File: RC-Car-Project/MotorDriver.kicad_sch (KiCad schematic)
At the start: 0 parts

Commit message: Add libraries and components in schs
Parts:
- added Q1, Q2: BTN8982TA, Package_TO_SOT_SMD:TO-263-7_TabPin8, symbol Power_Management:BTN8982TA
- added U9: SN74HC244PWR, PW20, symbol SN74HC244PWR:SN74HC244PWR
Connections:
- new net: Q2.4, Q2.8
- new net: Q1.4, Q1.8

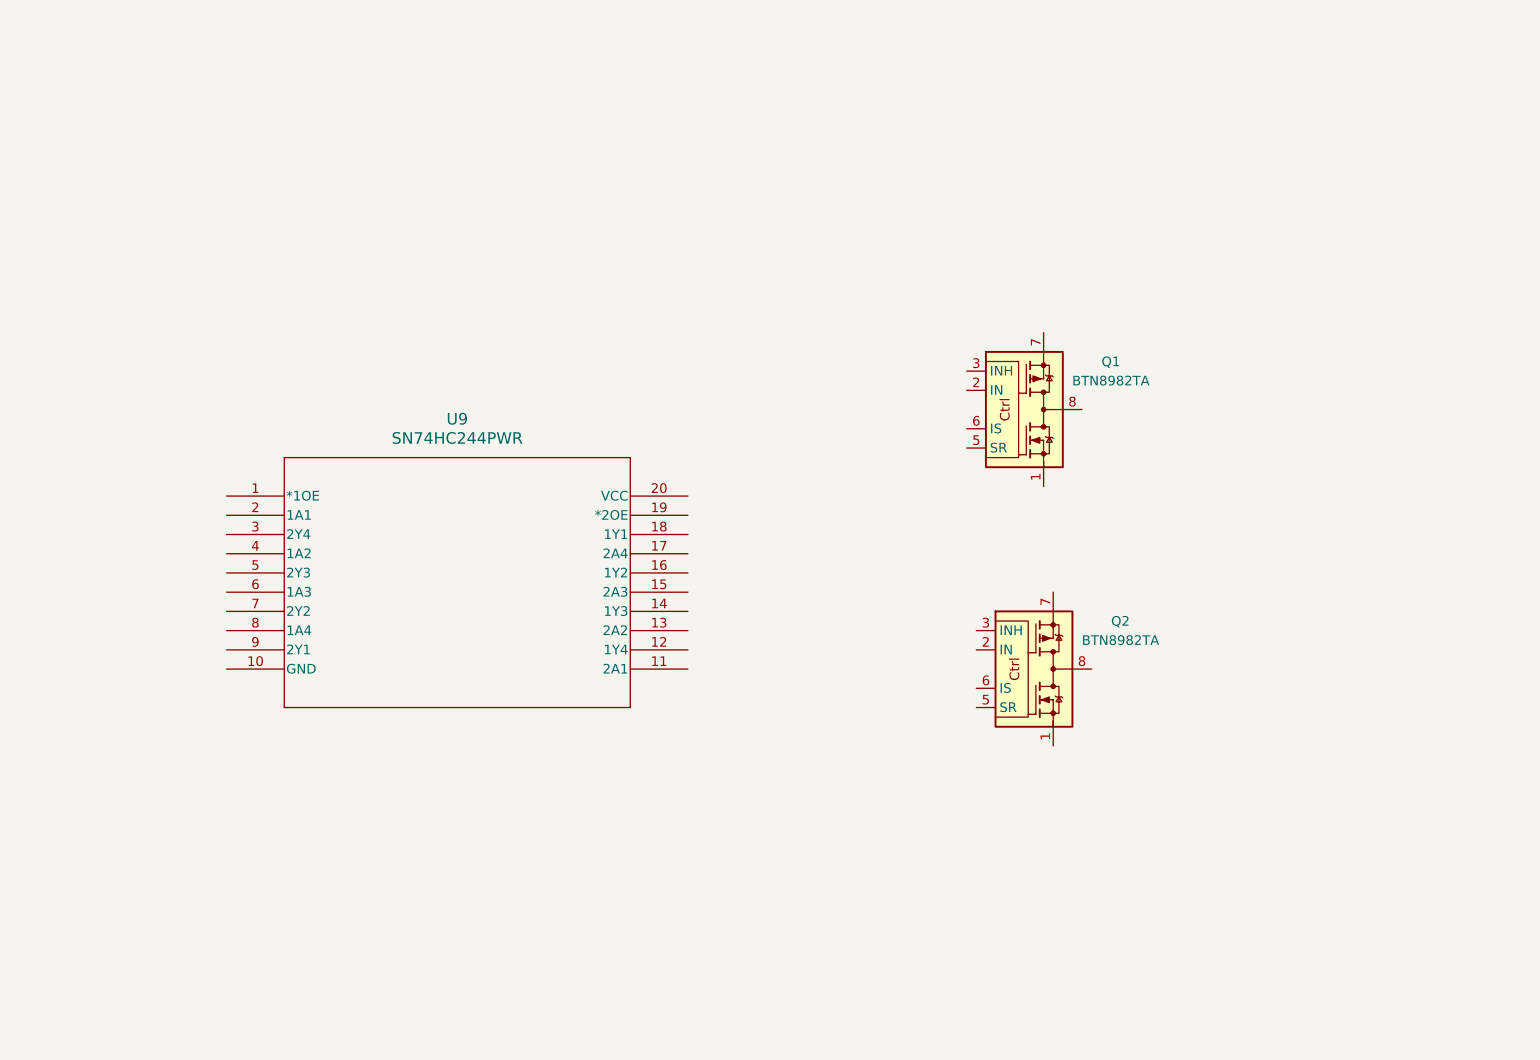
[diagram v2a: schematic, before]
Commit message: Added Basic Schematic + STM32 Project config. TODO: Component value selection + double check all connections.
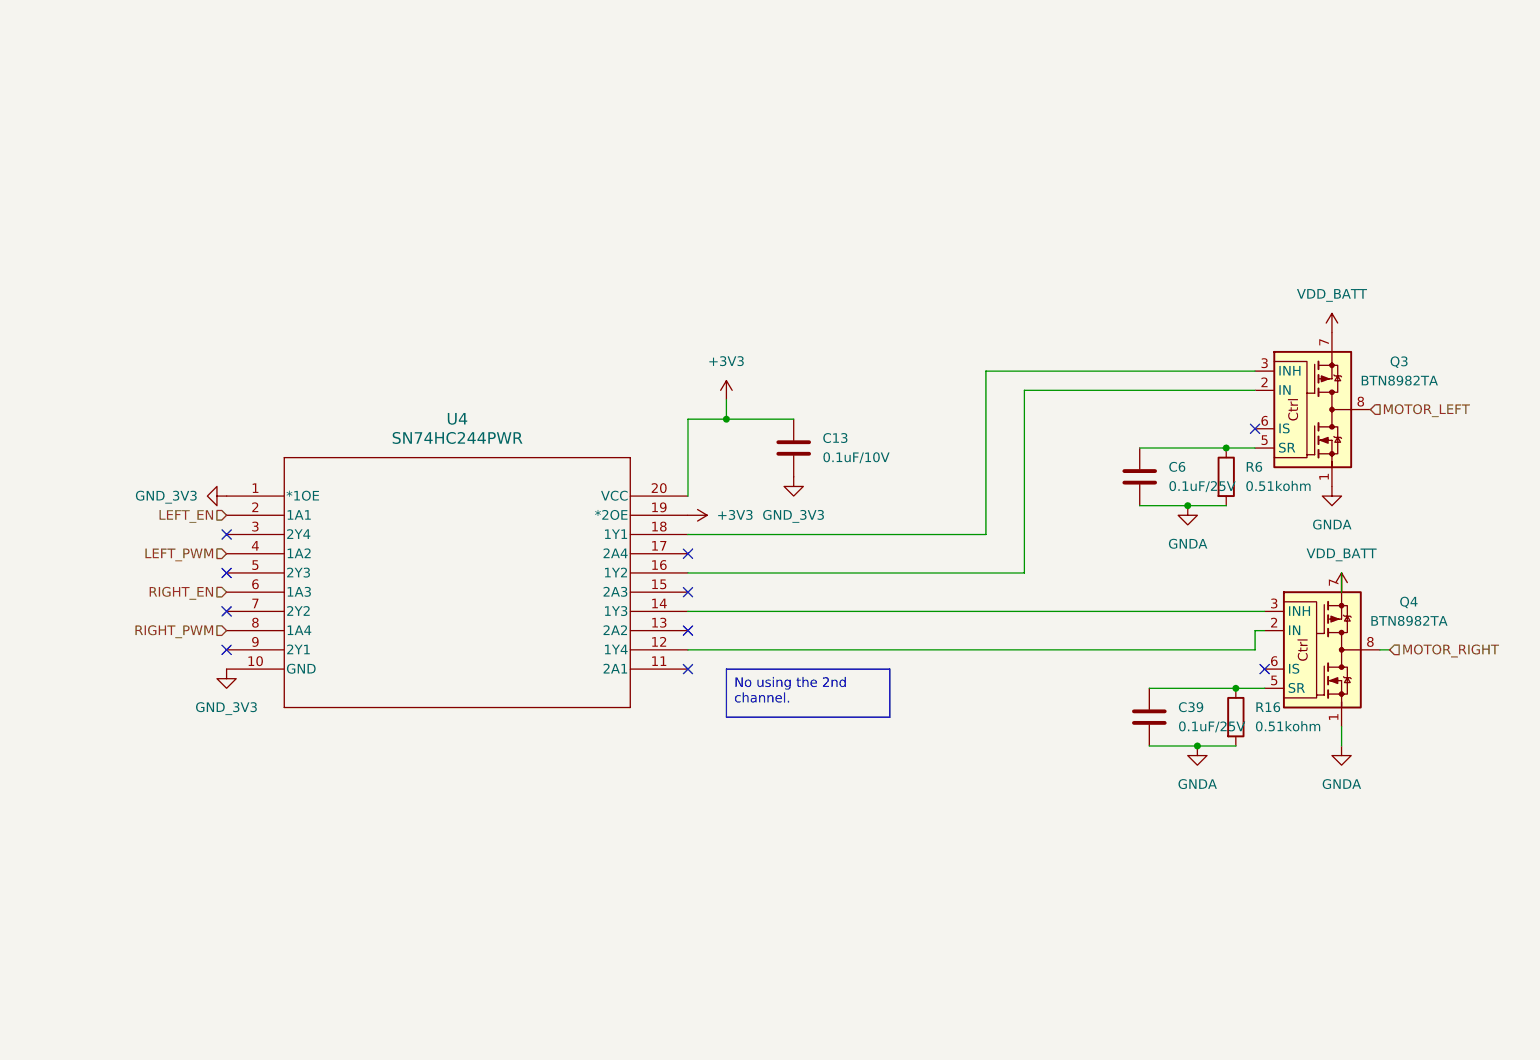
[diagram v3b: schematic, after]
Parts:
- added C13: 0.1uF/10V, symbol Device:C
- added C39, C6: 0.1uF/25V, symbol Device:C
- added R16, R6: 0.51kohm, symbol Device:R
- renumbered Q1 to Q3, Q2 to Q4, U9 to U4
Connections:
- net GNDA: now reaches Q4.1
- net GNDA: now also Q3.1, C39.2, C6.2, R16.2, R6.2
- net at Q4.2 (IN): now also U4.12 (1Y4)
- net at Q4.3 (INH): now also U4.14 (1Y3)
- net MOTOR_RIGHT: now reaches Q4.4, Q4.8
- net at Q4.5 (SR): now also C39.1, R16.1
- net VDD_BATT: now reaches Q4.7
- net VDD_BATT: now also Q3.7
- net at Q3.2 (IN): now also U4.16 (1Y2)
- net at Q3.3 (INH): now also U4.18 (1Y1)
- net MOTOR_LEFT: now reaches Q3.4, Q3.8
- net at Q3.5 (SR): now also C6.1, R6.1
- net GND_3V3: now reaches U4.1 (*1OE)
- net GND_3V3: now also U4.10 (GND), C13.2
- net +3V3: now reaches U4.19 (*2OE)
- net +3V3: now also U4.20 (VCC), C13.1
- net LEFT_EN: now reaches U4.2 (1A1)
- net LEFT_PWM: now reaches U4.4 (1A2)
- net RIGHT_EN: now reaches U4.6 (1A3)
- net RIGHT_PWM: now reaches U4.8 (1A4)
- no-connect marks 0 -> 10
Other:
- moved on the sheet: Q3, Q4

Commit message: Cleaned up Motor Circuit
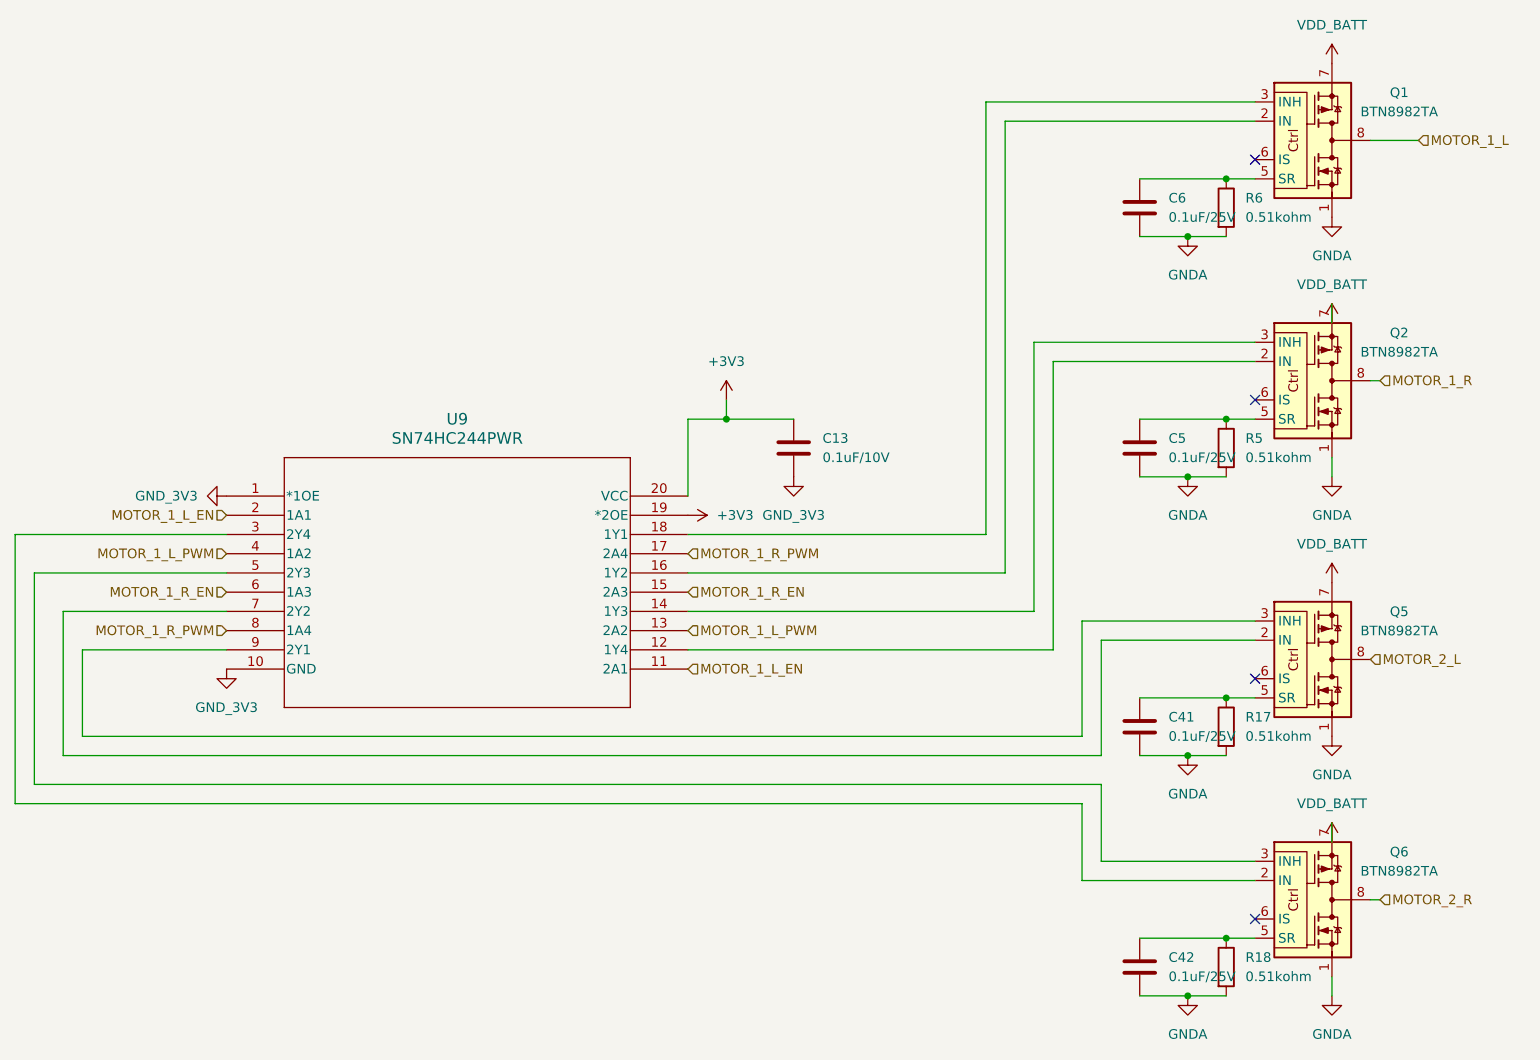
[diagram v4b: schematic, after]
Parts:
- added C41, C42: 0.1uF/25V, symbol Device:C
- added Q5, Q6: BTN8982TA, Package_TO_SOT_SMD:TO-263-7_TabPin8, symbol Power_Management:BTN8982TA
- added R17, R18: 0.51kohm, symbol Device:R
- renumbered C39 to C5, Q3 to Q1, Q4 to Q2, R16 to R5, U4 to U9
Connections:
- net LEFT_EN is gone; now on net MOTOR_1_L_EN: U9.2 (1A1)
- net LEFT_PWM is gone; now on net MOTOR_1_L_PWM: U9.4 (1A2)
- net RIGHT_EN is gone; now on net MOTOR_1_R_EN: U9.6 (1A3)
- net RIGHT_PWM is gone; now on net MOTOR_1_R_PWM: U9.8 (1A4)
- net GNDA: now also C41.2, C42.2, Q5.1, Q6.1, R17.2, R18.2
- net VDD_BATT: now also Q5.7, Q6.7
- net MOTOR_1_L_EN: now reaches U9.11 (2A1)
- net MOTOR_1_L_PWM: now reaches U9.13 (2A2)
- net MOTOR_1_R_EN: now reaches U9.15 (2A3)
- net MOTOR_1_R_PWM: now reaches U9.17 (2A4)
- net at U9.3 (2Y4): now also Q6.2 (IN)
- net at U9.5 (2Y3): now also Q6.3 (INH)
- net at U9.7 (2Y2): now also Q5.2 (IN)
- net at U9.9 (2Y1): now also Q5.3 (INH)
- net MOTOR_LEFT renamed MOTOR_1_L
- net MOTOR_RIGHT renamed MOTOR_1_R
- new net: C42.1, Q6.5 (SR), R18.1
- new net: C41.1, Q5.5 (SR), R17.1
- new net MOTOR_2_L: Q5.4, Q5.8
- new net MOTOR_2_R: Q6.4, Q6.8
- no-connect marks 10 -> 4
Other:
- moved on the sheet: C5, C6, Q1, Q2, R5, R6
